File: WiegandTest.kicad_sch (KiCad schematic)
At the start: 4 parts

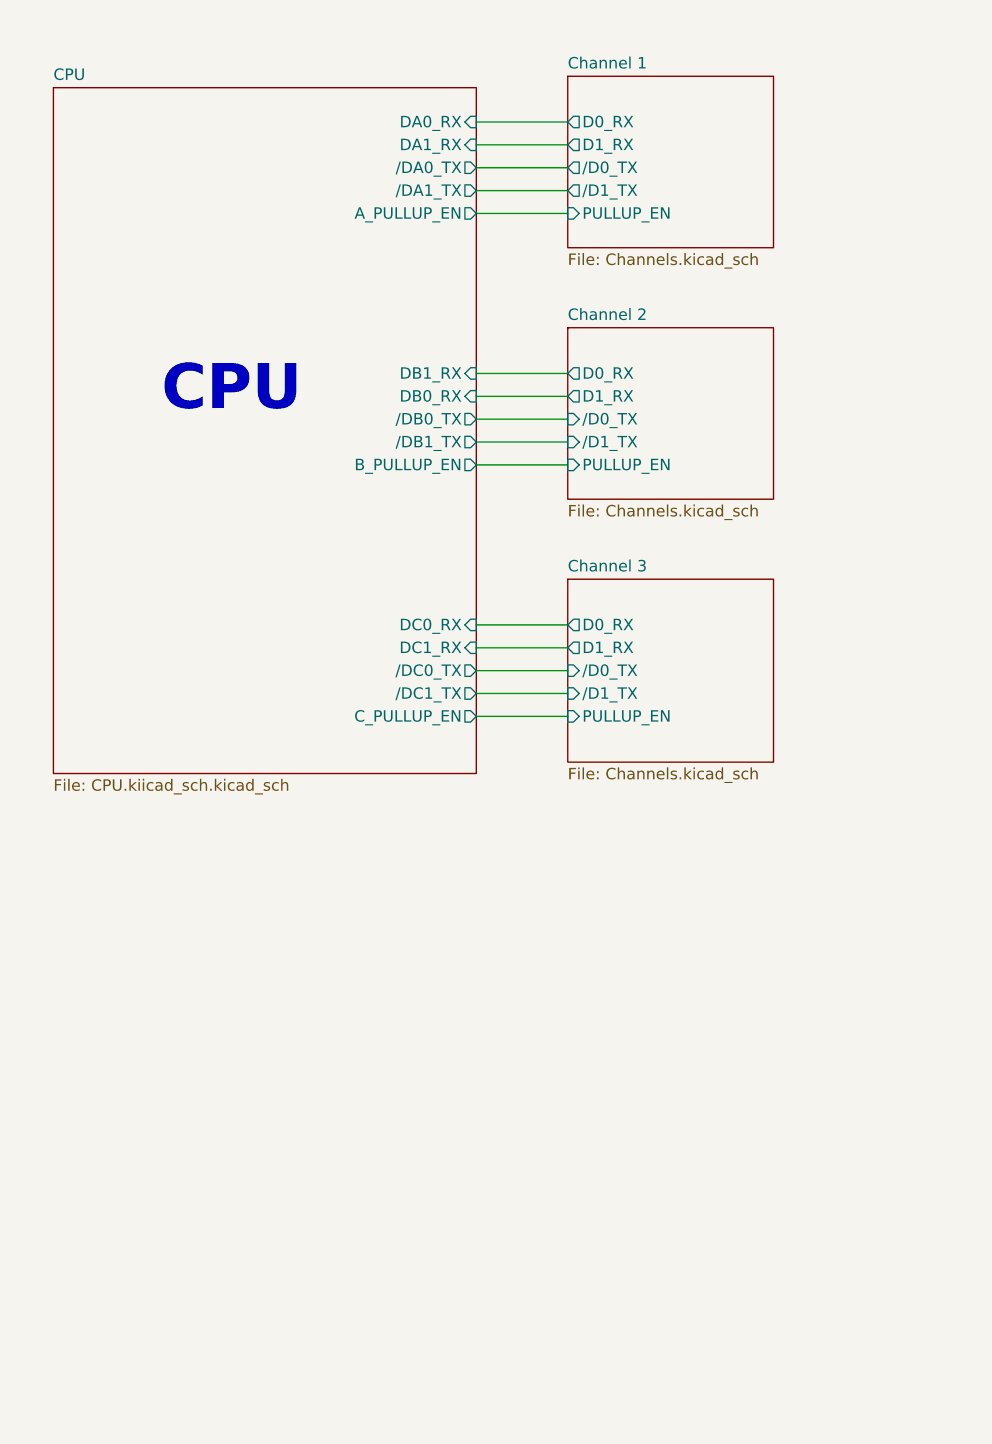
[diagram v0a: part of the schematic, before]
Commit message: OK, first basic layout complete - still need to do DRC and ERCs, get a good BOM going.
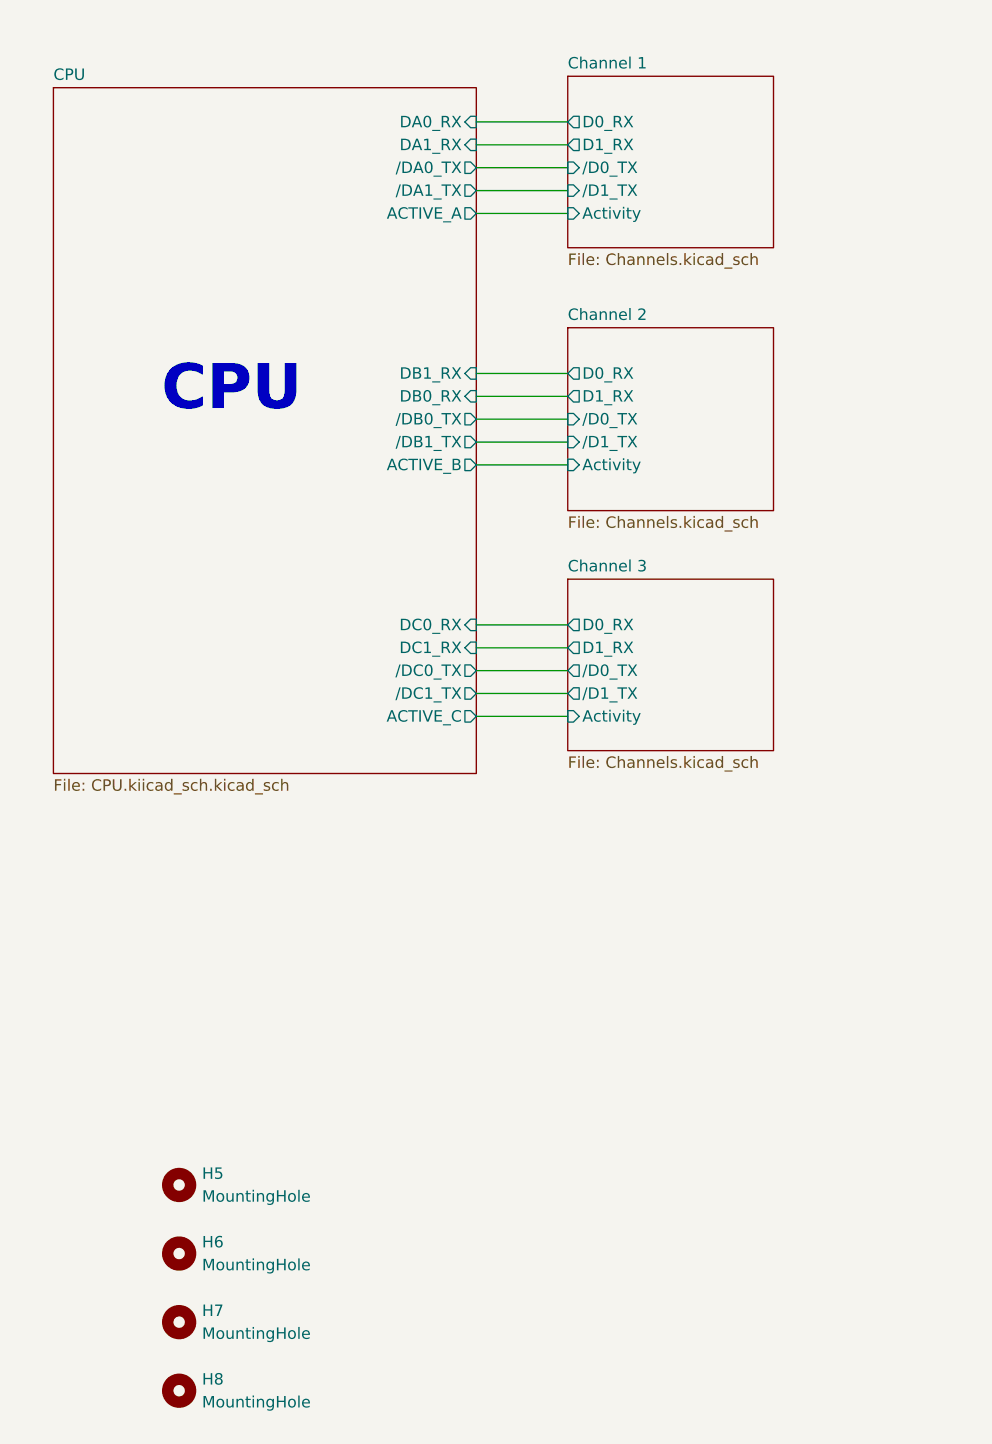
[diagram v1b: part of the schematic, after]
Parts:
- added H5, H6, H7, H8: MountingHole, MountingHole:MountingHole_2.5mm, symbol Mechanical:MountingHole
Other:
- sheet CPU ports: added ACTIVE_A, ACTIVE_B, ACTIVE_C; removed A_PULLUP_EN, B_PULLUP_EN, C_PULLUP_EN
- sheet Channel 1 ports: added Activity; removed PULLUP_EN
- sheet Channel 2 ports: added Activity; removed PULLUP_EN
- sheet Channel 3 ports: added Activity; removed PULLUP_EN

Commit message: No ERCs, No DRCs.  Excluded silkscreen past edge of board violations, not worth the time to fix.  Still need to complete BOM (MFG, MPN, on all parts)
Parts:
- added TP1, TP2: TestPoint, TestPoint:TestPoint_THTPad_1.5x1.5mm_Drill0.7mm, symbol Connector:TestPoint
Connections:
- new net GND: TP1.1, TP2.1

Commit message: BOM in schematic now completed via Digikey.  Board should be ready to build.
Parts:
- H1, H2, H3, H4, H5, H6, H7, H8, TP1, TP2: now not fitted
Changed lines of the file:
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@@
 		(in_bom no)
 		(on_board yes)
-		(dnp no)
+		(dnp yes)
 		(fields_autoplaced yes)
 		(property "Reference" "H5"
@@
 		(in_bom no)
 		(on_board yes)
-		(dnp no)
+		(dnp yes)
 		(fields_autoplaced yes)
 		(property "Reference" "H8"
@@
 		(in_bom no)
 		(on_board yes)
-		(dnp no)
+		(dnp yes)
 		(fields_autoplaced yes)
 		(property "Reference" "H4"
@@
 		(in_bom yes)
 		(on_board yes)
-		(dnp no)
+		(dnp yes)
 		(fields_autoplaced yes)
 		(property "Reference" "TP1"
@@
 		(in_bom no)
 		(on_board yes)
-		(dnp no)
+		(dnp yes)
 		(fields_autoplaced yes)
 		(property "Reference" "H3"
@@
 		(in_bom no)
 		(on_board yes)
-		(dnp no)
+		(dnp yes)
 		(fields_autoplaced yes)
 		(property "Reference" "H2"
@@
 		(in_bom yes)
 		(on_board yes)
-		(dnp no)
+		(dnp yes)
 		(fields_autoplaced yes)
 		(property "Reference" "TP2"
@@
 		(in_bom no)
 		(on_board yes)
-		(dnp no)
+		(dnp yes)
 		(fields_autoplaced yes)
 		(property "Reference" "H1"
@@
 		(in_bom no)
 		(on_board yes)
-		(dnp no)
+		(dnp yes)
 		(fields_autoplaced yes)
 		(property "Reference" "H6"
@@
 		(in_bom no)
 		(on_board yes)
-		(dnp no)
+		(dnp yes)
 		(fields_autoplaced yes)
 		(property "Reference" "H7"

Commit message: OK, Schematic is good for Rev B.  PCB not updated yet to match new schematic changes.
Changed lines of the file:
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@@
 	(paper "A4")
 	(title_block
-		(date "2025-11-10")
-		(rev "A")
+		(date "2025-12-19")
+		(rev "B")
 		(comment 1 "JPH")
 	)
@@
 			)
 		)
+		(pin "DB0_RX" input
+			(at 109.22 73.66 0)
+			(effects
+				(font
+					(size 1.27 1.27)
+				)
+				(justify right)
+			)
+		)
 		(pin "DB1_RX" input
-			(at 109.22 73.66 0)
-			(effects
-				(font
-					(size 1.27 1.27)
-				)
-				(justify right)
-			)
-		)
-		(pin "DB0_RX" input
 			(at 109.22 76.2 0)
 			(effects

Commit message: Fixed PCB.  Added new rev info to schematics.  No DRCs. Should be good to go at this time.
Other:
- note added: "Fixed multiple issues where pins could not be used for the functions they were assigned."
- note added: "Revision B 12/21/2025"
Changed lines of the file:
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@@
+		)
+	)
+	(text "Revision B  12/21/2025 "
+		(exclude_from_sim no)
+		(at 209.55 26.67 0)
+		(effects
+			(font
+				(size 1.27 1.27)
+			)
+		)
+	)
+	(text "Fixed multiple issues where pins could not \nbe used for the functions they were assigned."
+		(exclude_from_sim no)
+		(at 234.188 27.432 0)
+		(effects
+			(font
+				(size 1.27 1.27)
+			)
+			(justify left)
 		)
 	)

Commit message: This is Rev C, which is a smaller PCB where the LCD no longer fits on the board.  Still has the LCCD connector, though.
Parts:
- removed H5, H6, H7, H8: MountingHole, MountingHole:MountingHole_2.5mm, symbol Mechanical:MountingHole
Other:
- note added: "Made PCA smaller to fit test systems better, but LCD does not fit on board."
- note added: "Revision C 3/23/26"
